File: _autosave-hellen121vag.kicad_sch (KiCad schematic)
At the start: 31 parts, among them J21 Conn_01x05_Male, J22 USB_B_Mini, M1 Module-power_12and5V-0.3, M2 Module-knock-0.2, M3 Module-vr-discrete-0.5, M4 Module-vr-max9924-0.1, M5 Module-wbo-0.5, M6 Module:mega-mcu100/0.3, M7 Module-can-0.1, M8 Module-motor-driver-0.1, P1 368255-2, U10 BTS6143D

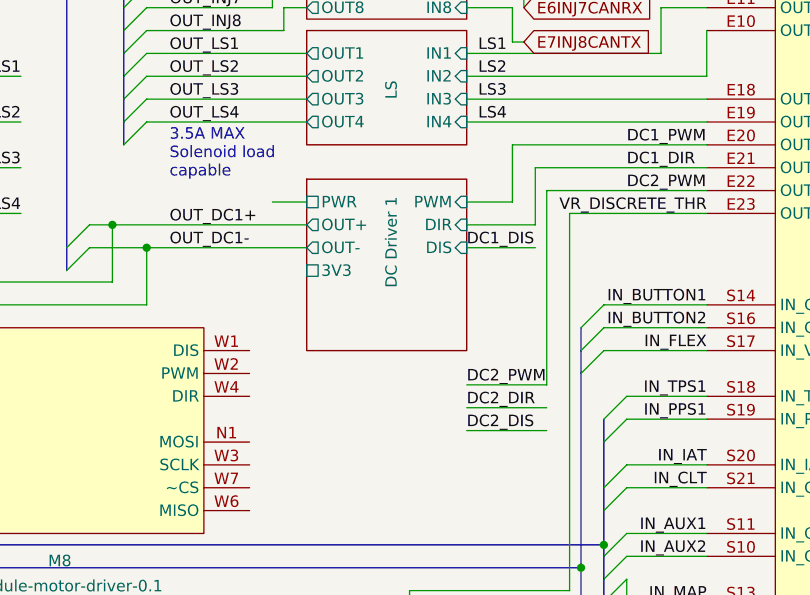
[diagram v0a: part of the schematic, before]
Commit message: se ha completado un 99% la colocacion de componentes y adapatacion
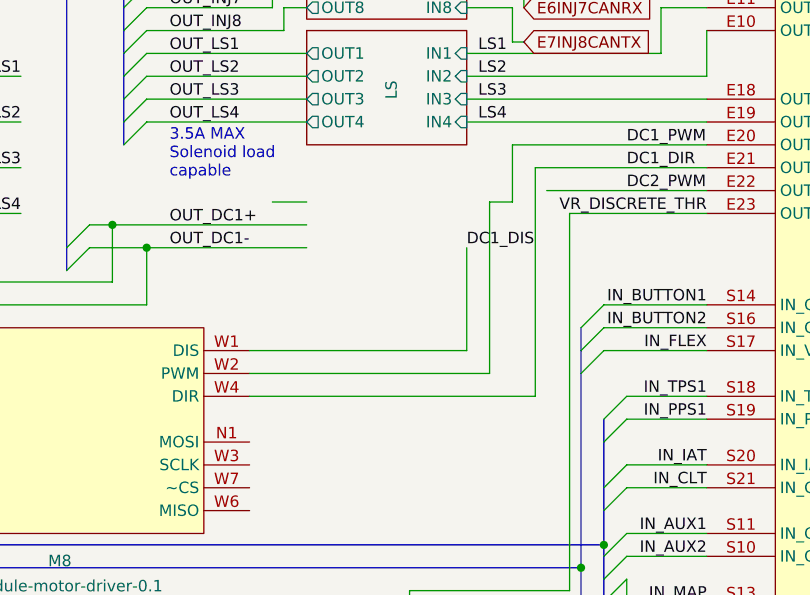
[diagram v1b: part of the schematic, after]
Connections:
- net DC1_DIR: now also M8.W4 (DIR)
- net DC1_DIS: now also M8.W1 (DIS)
- net DC1_PWM: now also M8.W2 (PWM)
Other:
- removed sheet DC Driver 1
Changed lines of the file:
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@@
 	(wire
 		(pts
+			(xy 279.4 196.85) (xy 279.4 177.8)
+		)
+		(stroke
+			(width 0)
+			(type default)
+		)
+	)
+	(wire
+		(pts
 			(xy 298.45 156.21) (xy 298.45 161.29)
 		)
@@
 	(wire
 		(pts
+			(xy 252.73 196.85) (xy 279.4 196.85)
+		)
+		(stroke
+			(width 0)
+			(type default)
+		)
+	)
+	(wire
+		(pts
 			(xy 300.99 106.68) (xy 300.99 118.11)
 		)
@@
 	(wire
 		(pts
+			(xy 279.4 177.8) (xy 281.94 177.8)
+		)
+		(stroke
+			(width 0)
+			(type default)
+		)
+	)
+	(wire
+		(pts
 			(xy 276.86 104.14) (xy 303.53 104.14)
 		)
@@
 	(wire
 		(pts
+			(xy 252.73 194.31) (xy 276.86 194.31)
+		)
+		(stroke
+			(width 0)
+			(type default)
+		)
+	)
+	(wire
+		(pts
 			(xy 400.05 133.35) (xy 400.05 130.81)
 		)
@@
 	(wire
 		(pts
-			(xy 276.86 182.88) (xy 284.48 182.88)
-		)
-		(stroke
-			(width 0)
-			(type default)
-		)
-	)
-	(wire
-		(pts
 			(xy 275.59 260.35) (xy 275.59 273.05)
 		)
@@
 	(wire
 		(pts
-			(xy 276.86 177.8) (xy 281.94 177.8)
-		)
-		(stroke
-			(width 0)
-			(type default)
-		)
-	)
-	(wire
-		(pts
 			(xy 294.64 209.55) (xy 303.53 209.55)
 		)
@@
 	(wire
 		(pts
-			(xy 276.86 198.12) (xy 285.75 198.12)
-		)
-		(stroke
-			(width 0)
-			(type default)
-		)
-	)
-	(wire
-		(pts
 			(xy 153.67 180.34) (xy 153.67 177.8)
 		)
@@
 	(wire
 		(pts
-			(xy 285.75 198.12) (xy 285.75 176.53)
-		)
-		(stroke
-			(width 0)
-			(type default)
-		)
-	)
-	(wire
-		(pts
 			(xy 288.29 179.07) (xy 303.53 179.07)
 		)
@@
 		)
 	)
-	(wire
-		(pts
-			(xy 276.86 203.2) (xy 285.75 203.2)
-		)
-		(stroke
-			(width 0)
-			(type default)
-		)
-	)
 	(bus
 		(pts
@@
 	(wire
 		(pts
-			(xy 276.86 180.34) (xy 284.48 180.34)
+			(xy 252.73 143.51) (xy 241.3 143.51)
 		)
 		(stroke
@@
 	(wire
 		(pts
-			(xy 252.73 143.51) (xy 241.3 143.51)
+			(xy 176.53 194.31) (xy 176.53 195.58)
 		)
 		(stroke
@@
 	(wire
 		(pts
-			(xy 176.53 194.31) (xy 176.53 195.58)
+			(xy 252.73 199.39) (xy 284.48 199.39)
 		)
 		(stroke
@@
 	(wire
 		(pts
-			(xy 284.48 180.34) (xy 284.48 173.99)
+			(xy 284.48 173.99) (xy 284.48 199.39)
 		)
 		(stroke
@@
 	(wire
 		(pts
+			(xy 276.86 194.31) (xy 276.86 182.88)
+		)
+		(stroke
+			(width 0)
+			(type default)
+		)
+	)
+	(wire
+		(pts
 			(xy 364.49 312.42) (xy 361.95 312.42)
 		)
@@
 	(wire
 		(pts
-			(xy 276.86 200.66) (xy 285.75 200.66)
-		)
-		(stroke
-			(width 0)
-			(type default)
-		)
-	)
-	(wire
-		(pts
 			(xy 241.3 166.37) (xy 259.08 166.37)
 		)
@@
 		)
 	)
-	(label "DC2_DIS"
-		(at 276.86 203.2 0)
-		(effects
-			(font
-				(size 1.27 1.27)
-			)
-			(justify left bottom)
-		)
-	)
 	(label "3_WBO_Heater"
 		(at 163.83 60.96 0)
@@
 		)
 	)
-	(label "DC2_PWM"
-		(at 276.86 198.12 0)
-		(effects
-			(font
-				(size 1.27 1.27)
-			)
-			(justify left bottom)
-		)
-	)
 	(label "VR_MAX9924"
 		(at 372.11 171.45 0)
@@
 		)
 	)
-	(label "DC2_DIR"
-		(at 276.86 200.66 0)
-		(effects
-			(font
-				(size 1.27 1.27)
-			)
-			(justify left bottom)
-		)
-	)
 	(label "MISO3"
 		(at 372.11 135.89 0)
@@
 				)
 			)
-		)
-	)
-	(sheet
-		(at 259.08 175.26)
-		(size 17.78 19.05)
-		(stroke
-			(width 0.1524)
-			(type solid)
-		)
-		(fill
-			(color 0 0 0 0.0000)
-		)
-		(property "Sheetname" "DC Driver 1"
-			(at 269.24 187.325 90)
-			(effects
-				(font
-					(size 1.27 1.27)
-				)
-				(justify left bottom)
-			)
-		)
-		(property "Sheetfile" "DC_MOTOR_0.1.kicad_sch"
-			(at 259.08 188.5446 0)
-			(effects
-				(font
-					(size 1.27 1.27)
-				)
-				(justify left top)
-				(hide yes)
-			)
-		)
-		(pin "OUT+" output
-			(at 259.08 180.34 180)
-			(effects
-				(font
-					(size 1.27 1.27)
-				)
-				(justify left)
-			)
-		)
-		(pin "OUT-" output
-			(at 259.08 182.88 180)
-			(effects
-				(font
-					(size 1.27 1.27)
-				)
-				(justify left)
-			)
-		)
-		(pin "PWR" passive
-			(at 259.08 177.8 180)
-			(effects
-				(font
-					(size 1.27 1.27)
-				)
-				(justify left)
-			)
-		)
-		(pin "PWM" input
-			(at 276.86 177.8 0)
-			(effects
-				(font
-					(size 1.27 1.27)
-				)
-				(justify right)
-			)
-		)
-		(pin "DIR" input
-			(at 276.86 180.34 0)
-			(effects
-				(font
-					(size 1.27 1.27)
-				)
-				(justify right)
-			)
-		)
-		(pin "DIS" input
-			(at 276.86 182.88 0)
-			(effects
-				(font
-					(size 1.27 1.27)
-				)
-				(justify right)
-			)
-		)
-		(pin "3V3" passive
-			(at 259.08 185.42 180)
-			(effects
-				(font
-					(size 1.27 1.27)
-				)
-				(justify left)
-			)
-		)
-		(instances
-			(project "hellen121vag"
-				(path "/45c1f041-3b7c-4036-abe9-e26621c05a73"
-					(page "2")
-				)
-			)
